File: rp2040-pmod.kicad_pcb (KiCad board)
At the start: 2 copper layers, 39.4 x 20.3 mm, 42 parts, among them J1 USB_C_Receptacle_USB2.0, J2 Conn_01x03, J3 Conn_02x06_Odd_Even, SW1 USB Boot, SW2 USER1, SW3 RESET, U1 W25Q32JVSS, U2 AP2112K-3.3, U3 LM66200, U4 RP2040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

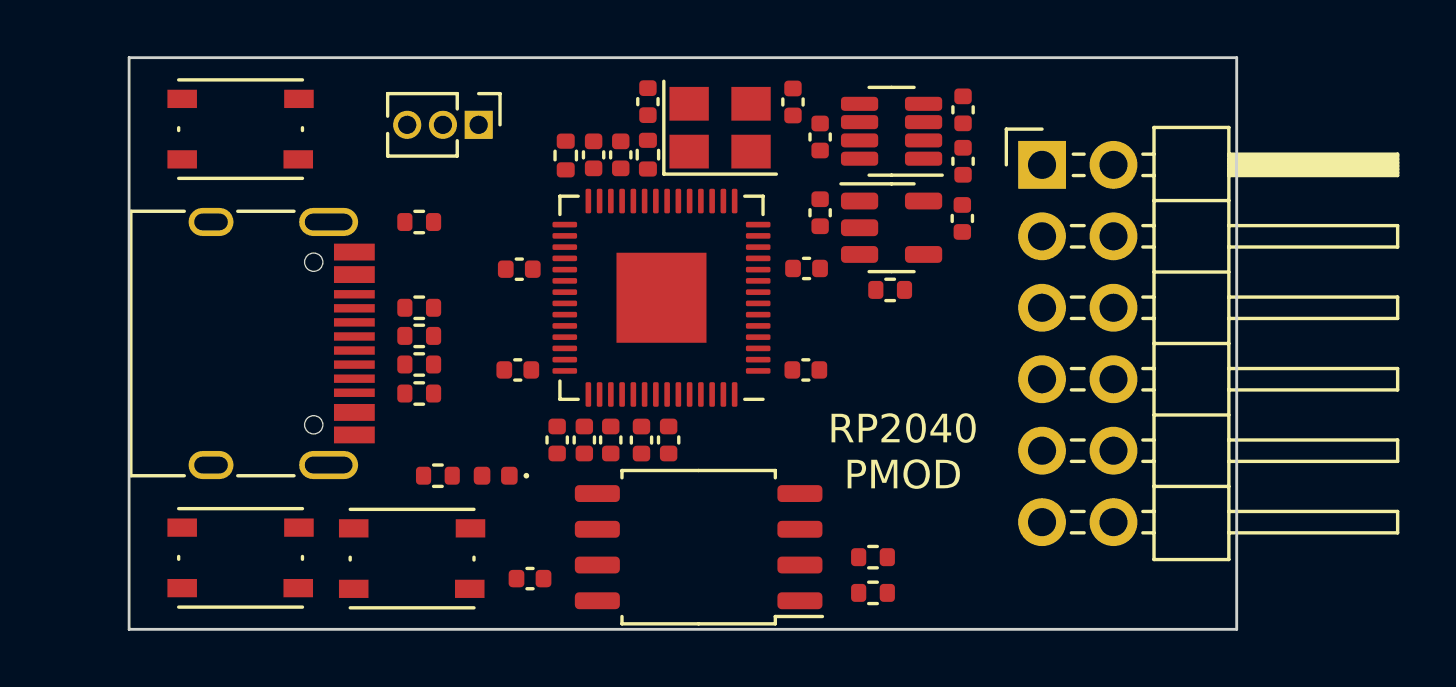
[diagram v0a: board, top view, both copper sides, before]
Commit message: Routed in 2 layers
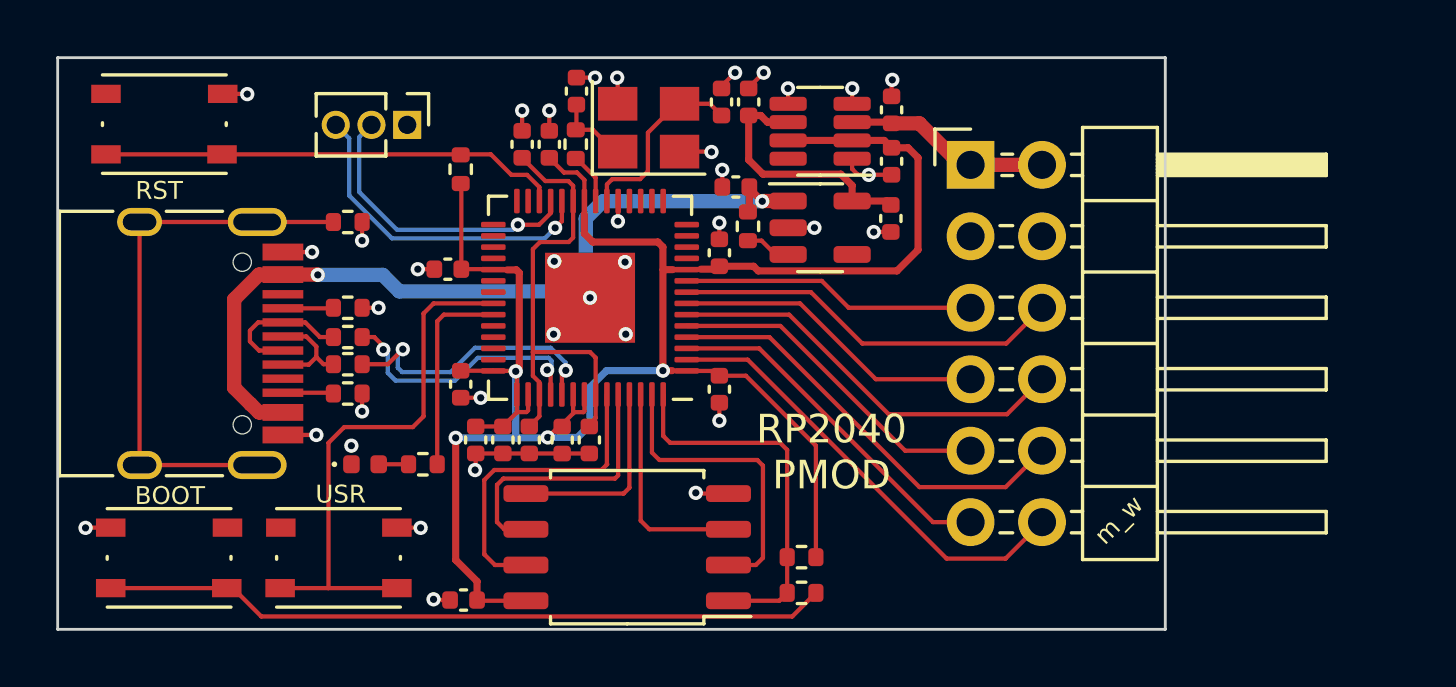
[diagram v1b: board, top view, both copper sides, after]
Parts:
- moved SW3 17.8 mm to (130.8, 83.6)
- moved SW2 15.6 mm to (137.0, 99.1), turned to 180 degrees
- moved R6 5.54 mm to (151.5, 87.3), turned to -90 degrees
- moved D1 4.66 mm to (137.9, 95.7), turned to 0 degrees
- moved R9 3.77 mm to (141.3, 85.2)
- moved C15 3.15 mm to (150.5, 93.1), turned to 90 degrees
- moved C16 3.15 mm to (150.5, 88.2), turned to -90 degrees
- moved C1 3.13 mm to (151.1, 85.9), turned to 0 degrees
- moved C10 2.90 mm to (143.8, 94.9)
- moved C12 2.90 mm to (142.8, 94.9)
- moved C17 2.90 mm to (141.9, 94.9)
- moved C7 2.83 mm to (151.6, 82.9), turned to -90 degrees
- moved C18 2.82 mm to (144.9, 94.9)
- moved C8 2.82 mm to (145.9, 94.9)
- moved R8 2.73 mm to (137.3, 92.2)
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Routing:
- net +3.3V: track 0.00 -> 76.2 mm, vias 0 -> 4
- net VBUS: track 0.00 -> 30.3 mm, vias 0 -> 2
- net GND: track 0.00 -> 27.7 mm, vias 0 -> 36
- net Net-(R2-Pad1): track 0.00 -> 25.8 mm
- net Net-(J1-PadS1): track 0.00 -> 19.7 mm
- net Net-(SW2-Pad1): track 0.00 -> 19.4 mm
- net +1V1: track 0.00 -> 17.1 mm
- net Net-(R9-Pad2): track 0.00 -> 16.4 mm
- net /GPIO0: track 0.00 -> 16.1 mm
- net /GPIO2: track 0.00 -> 15.4 mm
- net /GPIO4: track 0.00 -> 14.6 mm
- net /GPIO6: track 0.00 -> 13.9 mm
- net /QSPI_SS: track 0.00 -> 13.4 mm
- net /GPIO1: track 0.00 -> 12.6 mm
- net /GPIO3: track 0.00 -> 11.9 mm
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- added copper zone on B.Cu, net GND
- added copper zone on F.Cu, net GND
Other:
- board text added: "BOOT"
- board text added: "RST"
- board text added: "USR"
- board text added: "m_w"

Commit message: Switch to .1" debug header
Also add some silkscreen labels on the bottom.
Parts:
- J2: footprint Connector_PinHeader_1.27mm:PinHeader_1x03_P1.27mm_Vertical -> Connector_PinHeader_2.54mm:PinHeader_1x03_P2.54mm_Vertical
- moved J2 3.22 mm to (136.2, 83.2), turned to 90 degrees
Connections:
- J2 pad 1: GND -> /SWCLK
- J2 pad 2: Net-(J2-Pad2) -> GND
- J2 pad 3: Net-(J2-Pad3) -> /SWD
- U4 pad 24: Net-(J2-Pad3) -> /SWCLK
- U4 pad 25: Net-(J2-Pad2) -> /SWD
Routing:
- net /SWCLK: track 0.00 -> 12.6 mm, vias 0 -> 1
- net Net-(J2-Pad3): track 11.9 -> 0.00 mm, vias 1 -> 0
- net /SWD: track 0.00 -> 11.0 mm, vias 0 -> 1
- net Net-(J2-Pad2): track 10.6 -> 0.00 mm, vias 1 -> 0
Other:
- board text added: "+3.3"
- board text added: "0"
- board text added: "1"
- board text added: "2"
- board text added: "3"
- board text added: "4"
- board text added: "5"
- board text added: "6"
- board text added: "7"
- board text added: "DEBUG"
- board text added: "GND"
- board text added: "SWCLK"
- board text added: "SWD"

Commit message: Fix some new DRCs
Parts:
- moved R9 0.86 mm to (141.3, 86.1)
- moved J2 0.09 mm to (136.2, 83.2)
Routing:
- net +3.3V: track 76.2 -> 75.3 mm
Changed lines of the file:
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@@
   )
   (footprint "Resistor_SMD:R_0402_1005Metric" (layer "F.Cu")
-    (at 141.3256 85.2444 90)
+    (at 141.3256 86.106 90)
     (descr "Resistor SMD 0402 (1005 Metric), square (rectangular) end terminal, IPC_7351 nominal, (Body size source: IPC-SM-782 page 72, https://www.pcb-3d.com/wordpress/wp-content/uploads/ipc-sm-782a_amendment_1_and_2.pdf), generated with kicad-footprint-generator")
     (tags "resistor")
@@
   )
   (footprint "Connector_PinHeader_2.54mm:PinHeader_1x03_P2.54mm_Vertical" (layer "F.Cu")
-    (at 136.2456 83.185 90)
+    (at 136.159 83.185 90)
     (descr "Through hole straight pin header, 1x03, 2.54mm pitch, single row")
     (tags "Through hole pin header THT 1x03 2.54mm single row")
@@
   (segment (start 144.8562 94.3916) (end 145.36692 93.88088) (width 0.1524) (layer "F.Cu") (net 25))
   (segment (start 143.323 92.4398) (end 143.323 93.2519) (width 0.1524) (layer "F.Cu") (net 25))
-  (segment (start 141.3484 85.7772) (end 141.3256 85.7544) (width 0.1524) (layer "F.Cu") (net 25))
   (segment (start 142.9672 88.8144) (end 142.4855 88.8144) (width 0.1524) (layer "F.Cu") (net 25))
   (segment (start 143.6624 93.8784) (end 143.3348 93.8784) (width 0.1524) (layer "F.Cu") (net 25))
@@
   (segment (start 144.806231 94.3916) (end 144.419778 94.778053) (width 0.1524) (layer "F.Cu") (net 25))
   (segment (start 148.844 92.4052) (end 148.8532 92.4144) (width 0.1524) (layer "F.Cu") (net 25))
+  (segment (start 141.3484 88.7984) (end 141.3484 86.6388) (width 0.1524) (layer "F.Cu") (net 25))
   (segment (start 148.336 87.8332) (end 146.0246 87.8332) (width 0.254) (layer "F.Cu") (net 25))
   (segment (start 144.9324 94.3916) (end 144.806231 94.3916) (width 0.1524) (layer "F.Cu") (net 25))
@@
   (segment (start 151.90208 88.85928) (end 151.737 88.6942) (width 0.254) (layer "F.Cu") (net 25))
   (segment (start 145.69192 93.88088) (end 145.36692 93.88088) (width 0.1524) (layer "F.Cu") (net 25))
-  (segment (start 141.3484 88.7984) (end 141.3484 85.7772) (width 0.1524) (layer "F.Cu") (net 25))
   (segment (start 148.5138 92.4052) (end 148.5138 88.011) (width 0.254) (layer "F.Cu") (net 25))
   (segment (start 149.3605 88.8144) (end 148.869402 88.8144) (width 0.1524) (layer "F.Cu") (net 25))
@@
   (segment (start 148.5138 88.011) (end 148.336 87.8332) (width 0.254) (layer "F.Cu") (net 25))
   (segment (start 141.859 94.389) (end 142.8242 94.389) (width 0.1524) (layer "F.Cu") (net 25))
+  (segment (start 141.3484 86.6388) (end 141.3256 86.616) (width 0.1524) (layer "F.Cu") (net 25))
   (segment (start 145.723 85.6266) (end 145.45792 85.36152) (width 0.1524) (layer "F.Cu") (net 25))
   (segment (start 148.869402 88.8144) (end 148.8694 88.814402) (width 0.1524) (layer "F.Cu") (net 25))
@@
   (segment (start 145.323 86.3769) (end 145.323 87.676562) (width 0.1524) (layer "F.Cu") (net 40))
   (segment (start 143.764 94.389) (end 144.123 94.03) (width 0.1524) (layer "F.Cu") (net 40))
-  (segment (start 144.123 85.883774) (end 143.684826 85.4456) (width 0.1524) (layer "F.Cu") (net 41))
+  (segment (start 132.842 84.7172) (end 133.7228 85.598) (width 0.1524) (layer "F.Cu") (net 41))
+  (segment (start 133.7228 85.598) (end 143.837226 85.598) (width 0.1524) (layer "F.Cu") (net 41))
   (segment (start 128.717 84.7172) (end 132.842 84.7172) (width 0.1524) (layer "F.Cu") (net 41))
-  (segment (start 143.684826 85.4456) (end 143.127 85.4456) (width 0.1524) (layer "F.Cu") (net 41))
-  (segment (start 142.3986 84.7172) (end 143.127 85.4456) (width 0.1524) (layer "F.Cu") (net 41))
-  (segment (start 144.123 86.3769) (end 144.123 85.883774) (width 0.1524) (layer "F.Cu") (net 41))
-  (segment (start 132.842 84.7172) (end 142.3986 84.7172) (width 0.1524) (layer "F.Cu") (net 41))
+  (segment (start 143.837226 85.598) (end 144.123 85.883774) (width 0.1524) (layer "F.Cu") (net 41))
+  (segment (start 144.123 85.883774) (end 144.123 86.3769) (width 0.1524) (layer "F.Cu") (net 41))
   (segment (start 140.0048 94.0308) (end 139.6238 94.4118) (width 0.1524) (layer "F.Cu") (net 50))
   (segment (start 140.3636 90.0144) (end 140.0048 90.3732) (width 0.1524) (layer "F.Cu") (net 50))
@@
   (via (at 144.682857 87.329657) (size 0.508) (drill 0.254) (layers "F.Cu" "B.Cu") (net 61))
   (segment (start 138.861311 87.705711) (end 138.4554 87.2998) (width 0.1524) (layer "B.Cu") (net 61))
+  (segment (start 138.4554 87.2998) (end 138.4554 85.3948) (width 0.1524) (layer "B.Cu") (net 61))
+  (segment (start 143.565187 87.702411) (end 143.561887 87.705711) (width 0.1524) (layer "B.Cu") (net 61))
   (segment (start 144.310103 87.702411) (end 143.565187 87.702411) (width 0.1524) (layer "B.Cu") (net 61))
+  (segment (start 143.561887 87.705711) (end 138.861311 87.705711) (width 0.1524) (layer "B.Cu") (net 61))
+  (segment (start 136.2456 83.185) (end 136.159 83.185) (width 0.1524) (layer "B.Cu") (net 61))
   (segment (start 144.682857 87.329657) (end 144.310103 87.702411) (width 0.1524) (layer "B.Cu") (net 61))
   (segment (start 138.4554 85.3948) (end 136.2456 83.185) (width 0.1524) (layer "B.Cu") (net 61))
-  (segment (start 143.565187 87.702411) (end 143.561887 87.705711) (width 0.1524) (layer "B.Cu") (net 61))
-  (segment (start 143.561887 87.705711) (end 138.861311 87.705711) (width 0.1524) (layer "B.Cu") (net 61))
-  (segment (start 138.4554 87.2998) (end 138.4554 85.3948) (width 0.1524) (layer "B.Cu") (net 61))
   (segment (start 144.11501 87.2236) (end 144.527589 86.811021) (width 0.1524) (layer "F.Cu") (net 62))
   (segment (start 144.527589 86.811021) (end 144.527589 86.3802) (width 0.1524) (layer "F.Cu") (net 62))
   (segment (start 143.362189 87.2236) (end 144.11501 87.2236) (width 0.1524) (layer "F.Cu") (net 62))
   (via (at 143.362189 87.2236) (size 0.508) (drill 0.254) (layers "F.Cu" "B.Cu") (net 62))
+  (segment (start 141.239 83.2716) (end 138.9888 85.5218) (width 0.1524) (layer "B.Cu") (net 62))
   (segment (start 139.2682 87.2236) (end 143.362189 87.2236) (width 0.1524) (layer "B.Cu") (net 62))
+  (segment (start 141.239 83.185) (end 141.239 83.2716) (width 0.1524) (layer "B.Cu") (net 62))
   (segment (start 138.9888 85.5218) (end 138.9888 86.9442) (width 0.1524) (layer "B.Cu") (net 62))
   (segment (start 138.9888 86.9442) (end 139.2682 87.2236) (width 0.1524) (layer "B.Cu") (net 62))
-  (segment (start 141.3256 83.185) (end 138.9888 85.5218) (width 0.1524) (layer "B.Cu") (net 62))
   (zone (net 1) (net_name "GND") (layers F&B.Cu) (hatch edge 0.508)
     (connect_pads (clearance 0.254))

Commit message: Update LM66200 footprint
The footprint used was the wrong pitch and width. :(
New footprint is close enough to the datasheet to actually work. :)
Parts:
- U3: footprint Package_TO_SOT_SMD:SOT-23-8 -> rp2040-pmod:SOT-5x3
- moved U3 0.26 mm to (154.1, 83.6)
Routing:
- net GND: track 27.7 -> 28.6 mm

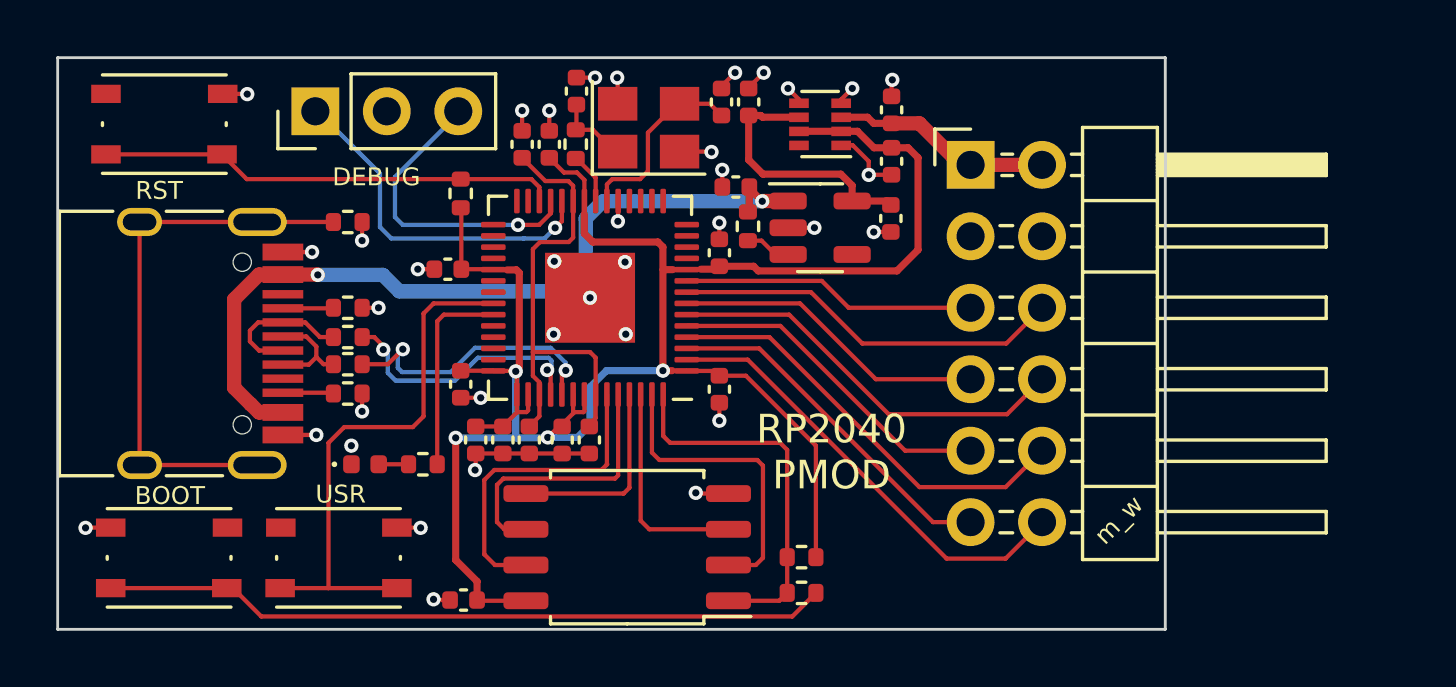
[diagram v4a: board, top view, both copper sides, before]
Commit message: Switch flash, add ADC header, add PMOD power detection
USON pattern swiped from emeb's library.

https://github.com/emeb/KiCad_Libs
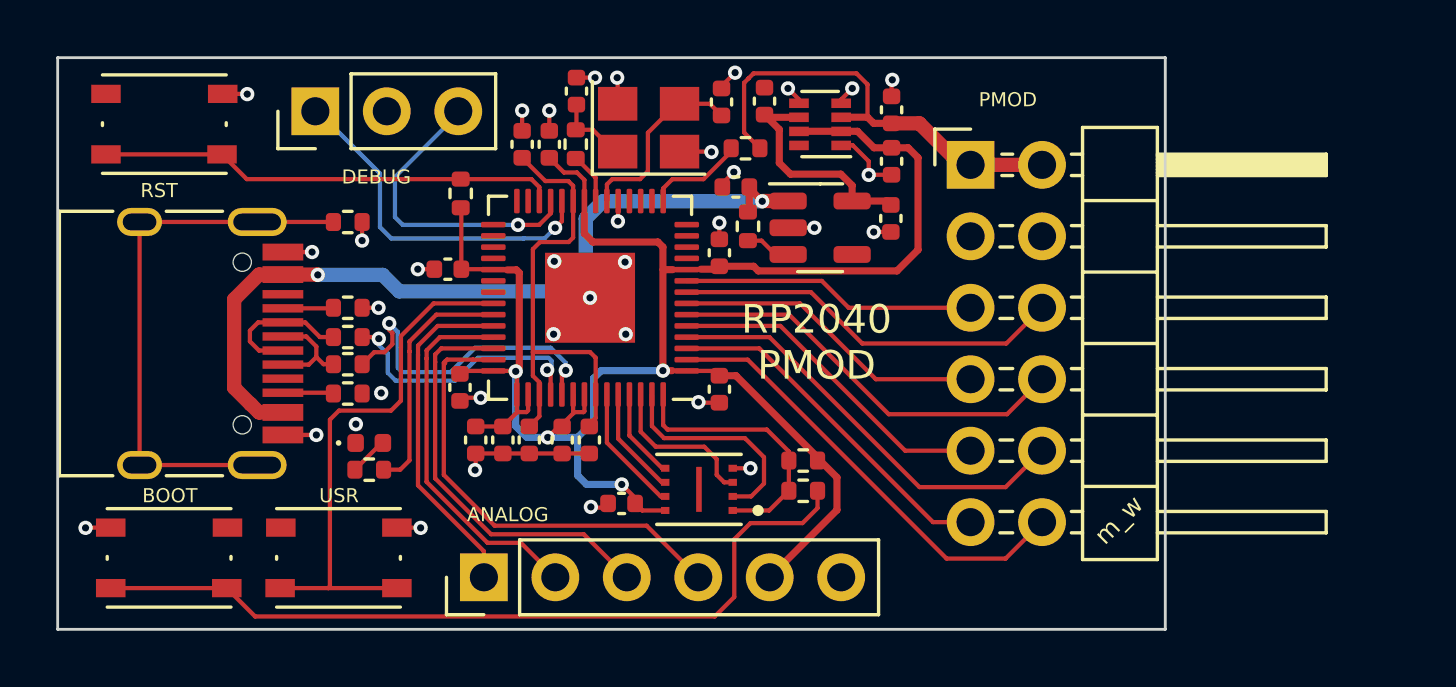
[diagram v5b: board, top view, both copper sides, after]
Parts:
- added J4: Conn_01x06, Connector_PinHeader_2.54mm:PinHeader_1x06_P2.54mm_Vertical, F.Cu at (142.2, 99.8)
- added R12: 10K, Resistor_SMD:R_0402_1005Metric, F.Cu at (151.4, 84.5)
- U1: value W25Q32JVSS -> W25Q16JVUXIQ; footprint Package_SO:SOIC-8_5.23x5.23mm_P1.27mm -> rp2040-pmod:USON-8_2x3
- moved C2 6.58 mm to (147.0, 97.1)
- moved R2 3.63 mm to (153.5, 96.7)
- moved R3 3.44 mm to (153.5, 95.6)
- moved U1 3.28 mm to (149.8, 96.6)
- moved R11 1.92 mm to (138.1, 95.9)
- moved D1 0.77 mm to (138.1, 95.0)
- moved C7 0.56 mm to (152.1, 82.8)
- moved C19 0.12 mm to (141.3, 93.0)
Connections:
- U4 pad 15: unconnected-(U4-Pad15) -> Net-(U4-Pad15)
- U4 pad 38: unconnected-(U4-Pad38) -> /ADC0
- U4 pad 39: unconnected-(U4-Pad39) -> /ADC1
- U4 pad 40: unconnected-(U4-Pad40) -> /ADC2
- U4 pad 41: unconnected-(U4-Pad41) -> /ADC3
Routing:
- net /ADC3: track 0.00 -> 16.4 mm
- net /ADC2: track 0.00 -> 14.8 mm
- net /ADC1: track 0.00 -> 13.2 mm
- net /ADC0: track 0.00 -> 12.2 mm
- net +3.3VP: track 7.84 -> 16.3 mm
- net /QSPI_SD3: track 11.4 -> 4.58 mm
- net /QSPI_SCLK: track 9.78 -> 3.89 mm
- net /QSPI_SD0: track 7.08 -> 3.21 mm
- net /QSPI_SS: track 13.4 -> 9.63 mm
- net Net-(U4-Pad15): track 0.00 -> 3.53 mm
- net Net-(R2-Pad1): track 25.8 -> 29.0 mm
- net +3.3V: track 75.1 -> 72.0 mm
- net /QSPI_SD1: track 10.8 -> 7.80 mm
- net /QSPI_SD2: track 7.73 -> 5.67 mm
- net GND: track 28.6 -> 26.9 mm, vias 36 -> 35
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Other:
- board text added: "ADC"
- board text added: "ANALOG"
- board text added: "DBG"
- board text added: "PMOD"
- board text added: "VREF"

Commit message: Silkscreen updates
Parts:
- added kibuzzard-6385637E: G***, kibuzzard-6385637E, F.Cu at (154.7, 92.5)
- added kibuzzard-6385637E: G***, kibuzzard-6385637E, B.Cu at (149.6, 89.8)
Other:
- board text added: "(\/) (oo) (__)"
- board text added: "(\__/) ( . _ .) / >"
- board text added: "(\__/) ( . _ .) / > $"
- board text added: "/\_/\ ( o.o ) > ^ <"
- board text added: ":0"
- board text added: "B^)"
- board text removed: "DBG"
- board text removed: "RP2040 PMOD"
